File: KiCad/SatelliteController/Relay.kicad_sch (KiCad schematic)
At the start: 47 parts, among them J1 RELAY_POWER, J13 CONN_SORENOID_VALVE, Q10 AO3400A, Q11 AO3400A, Q12 AO3400A, Q4 AO3400A, Q5 AO3400A, Q6 AO3400A, Q7 AO3400A, Q8 AO3400A, Q9 AO3400A, U9 MCP3208

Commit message: ガーバーファイルを再生成
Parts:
- J13: footprint TSRP_Connector_Hirose:DF11B-8DP-2DS -> TSRP_Connector_Hirose:DF51A-8DP-2DS
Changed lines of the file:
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@@
       (effects (font (size 1.27 1.27)))
     )
-    (property "Footprint" "TSRP_Connector_Hirose:DF11B-8DP-2DS" (at 62.23 74.93 0)
+    (property "Footprint" "TSRP_Connector_Hirose:DF51A-8DP-2DS" (at 62.23 74.93 0)
       (effects (font (size 1.27 1.27)) hide)
     )

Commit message: 抵抗値を修正
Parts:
- R23: value 200R -> 120R
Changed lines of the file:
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@@
       (effects (font (size 1.27 1.27)))
     )
-    (property "Value" "200R" (at 39.37 36.83 90)
+    (property "Value" "120R" (at 39.37 36.83 90)
       (effects (font (size 1.27 1.27)))
     )
@@
       (effects (font (size 1.27 1.27)))
     )
-    (property "Value" "200R" (at 171.45 115.57 90)
+    (property "Value" "120R" (at 171.45 115.57 90)
       (effects (font (size 1.27 1.27)))
     )
@@
       (effects (font (size 1.27 1.27)))
     )
-    (property "Value" "200R" (at 106.68 53.34 90)
+    (property "Value" "120R" (at 106.68 53.34 90)
       (effects (font (size 1.27 1.27)))
     )
@@
       (effects (font (size 1.27 1.27)))
     )
-    (property "Value" "200R" (at 171.45 53.34 90)
+    (property "Value" "120R" (at 171.45 53.34 90)
       (effects (font (size 1.27 1.27)))
     )
@@
       (effects (font (size 1.27 1.27)))
     )
-    (property "Value" "200R" (at 232.41 115.57 90)
+    (property "Value" "120R" (at 232.41 115.57 90)
       (effects (font (size 1.27 1.27)))
     )
@@
       (effects (font (size 1.27 1.27)))
     )
-    (property "Value" "200R" (at 128.27 170.18 90)
+    (property "Value" "120R" (at 128.27 170.18 90)
       (effects (font (size 1.27 1.27)))
     )
@@
       (effects (font (size 1.27 1.27)))
     )
-    (property "Value" "200R" (at 232.41 53.34 90)
+    (property "Value" "120R" (at 232.41 53.34 90)
       (effects (font (size 1.27 1.27)))
     )
@@
       (effects (font (size 1.27 1.27)))
     )
-    (property "Value" "200R" (at 106.68 115.57 90)
+    (property "Value" "120R" (at 106.68 115.57 90)
       (effects (font (size 1.27 1.27)))
     )
@@
       (effects (font (size 1.27 1.27)))
     )
-    (property "Value" "200R" (at 69.85 170.18 90)
-      (effects (font (size 1.27 1.27)))
-    )
+    (property "Value" "120R" (at 69.85 170.18 90)
+      (effects (font (size 1.27 1.27)))
+    )

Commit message: サテコンの制御スイッチをプルダウンに変更
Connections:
- net CTL_PURGE renamed LED_PURGE
- net CTL_SAFETY renamed LED_SAFTEY
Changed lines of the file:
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@@
+    (stroke (width 0) (type default))
+  )
+  (wire (pts (xy 34.29 39.37) (xy 36.83 39.37))
     (stroke (width 0) (type default))
   )
@@
     (stroke (width 0) (type default))
   )
-  (wire (pts (xy 34.29 39.37) (xy 36.83 39.37))
-    (stroke (width 0) (type default))
-  )
   (wire (pts (xy 62.23 106.68) (xy 64.77 106.68))
     (stroke (width 0) (type default))
@@
     )
   )
-  (global_label "CTL_SAFETY" (shape input) (at 34.29 39.37 180) (fields_autoplaced)
-    (effects (font (size 1.27 1.27)) (justify right))
-    (property "Intersheetrefs" "${INTERSHEET_REFS}" (at 20.559 39.37 0)
-      (effects (font (size 1.27 1.27)) (justify right) hide)
-    )
-  )
   (global_label "VREF_FILL" (shape output) (at 184.15 38.1 180) (fields_autoplaced)
     (effects (font (size 1.27 1.27)) (justify right))
@@
     )
   )
+  (global_label "LED_PURGE" (shape input) (at 123.19 172.72 180) (fields_autoplaced)
+    (effects (font (size 1.27 1.27)) (justify right))
+    (property "Intersheetrefs" "${INTERSHEET_REFS}" (at 109.58 172.72 0)
+      (effects (font (size 1.27 1.27)) (justify right) hide)
+    )
+  )
   (global_label "CTL_OPEN" (shape input) (at 227.33 118.11 180) (fields_autoplaced)
     (effects (font (size 1.27 1.27)) (justify right))
@@
     )
   )
+  (global_label "LED_SAFTEY" (shape input) (at 34.29 39.37 180) (fields_autoplaced)
+    (effects (font (size 1.27 1.27)) (justify right))
+    (property "Intersheetrefs" "${INTERSHEET_REFS}" (at 20.3776 39.37 0)
+      (effects (font (size 1.27 1.27)) (justify right) hide)
+    )
+  )
   (global_label "SPI_SCK" (shape input) (at 64.77 106.68 0) (fields_autoplaced)
     (effects (font (size 1.27 1.27)) (justify left))
@@
       (effects (font (size 1.27 1.27)) (justify right) hide)
     )
-  )
-  (global_label "CTL_PURGE" (shape input) (at 123.19 172.72 180) (fields_autoplaced)
-    (effects (font (size 1.27 1.27)) (justify right))
-    (property "Intersheetrefs" "${INTERSHEET_REFS}" (at 109.7614 172.72 0)
-      (effects (font (size 1.27 1.27)) (justify right) hide)
-    )

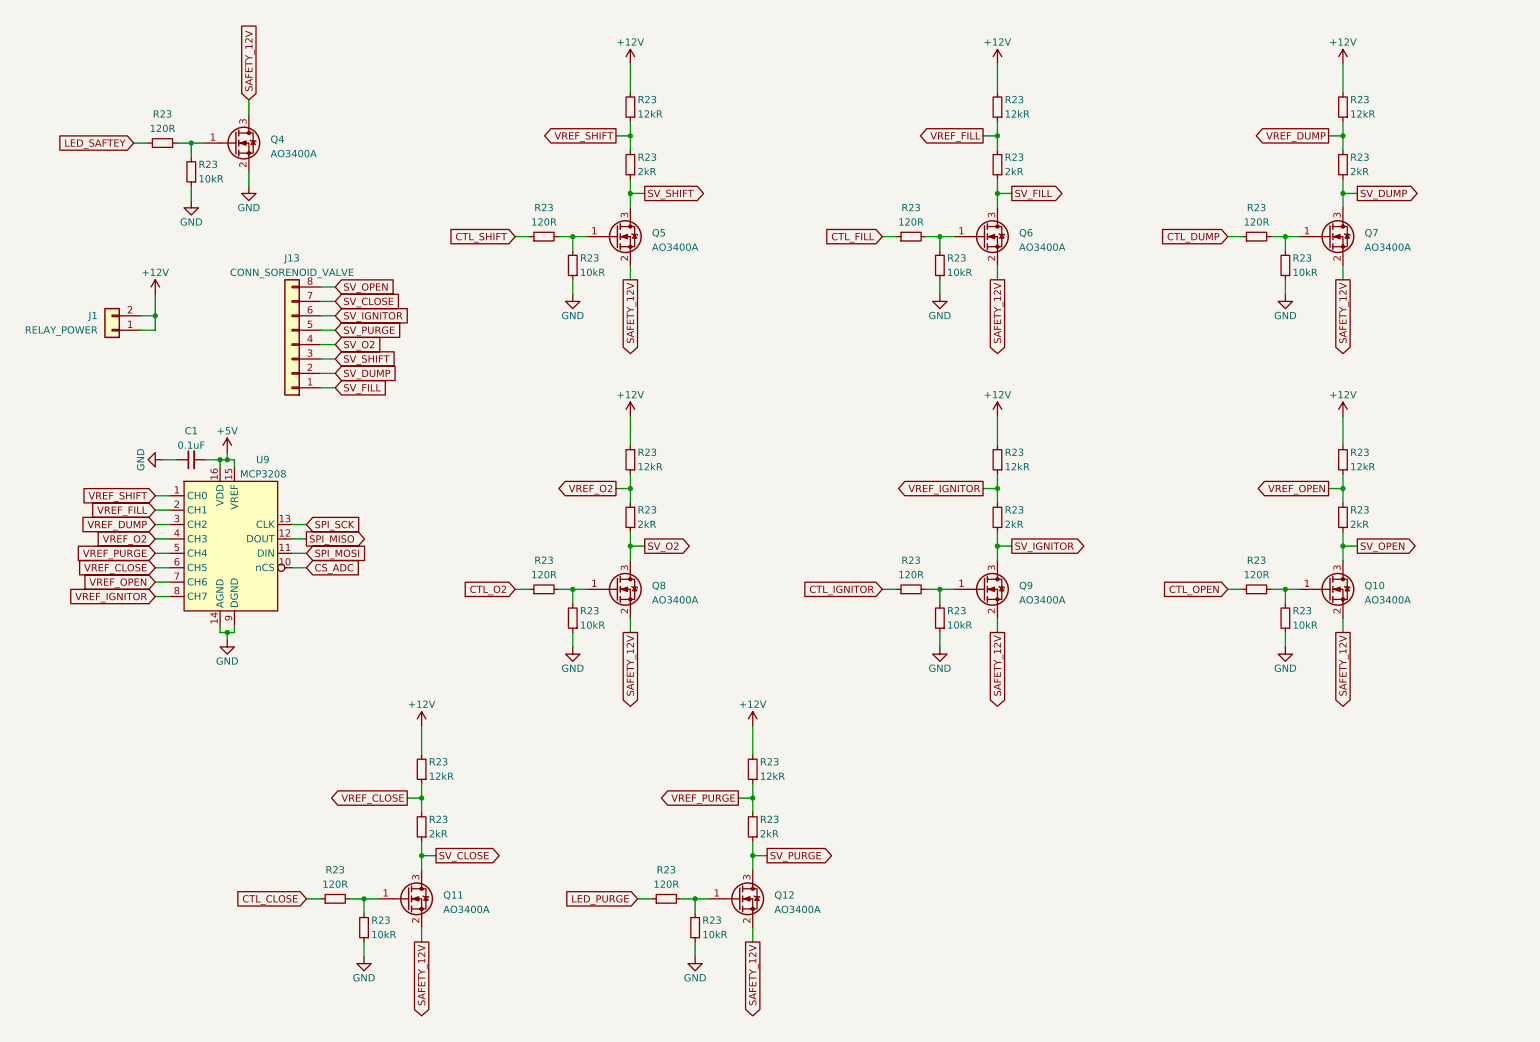
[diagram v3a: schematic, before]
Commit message: サテコンのオープン検知を修正
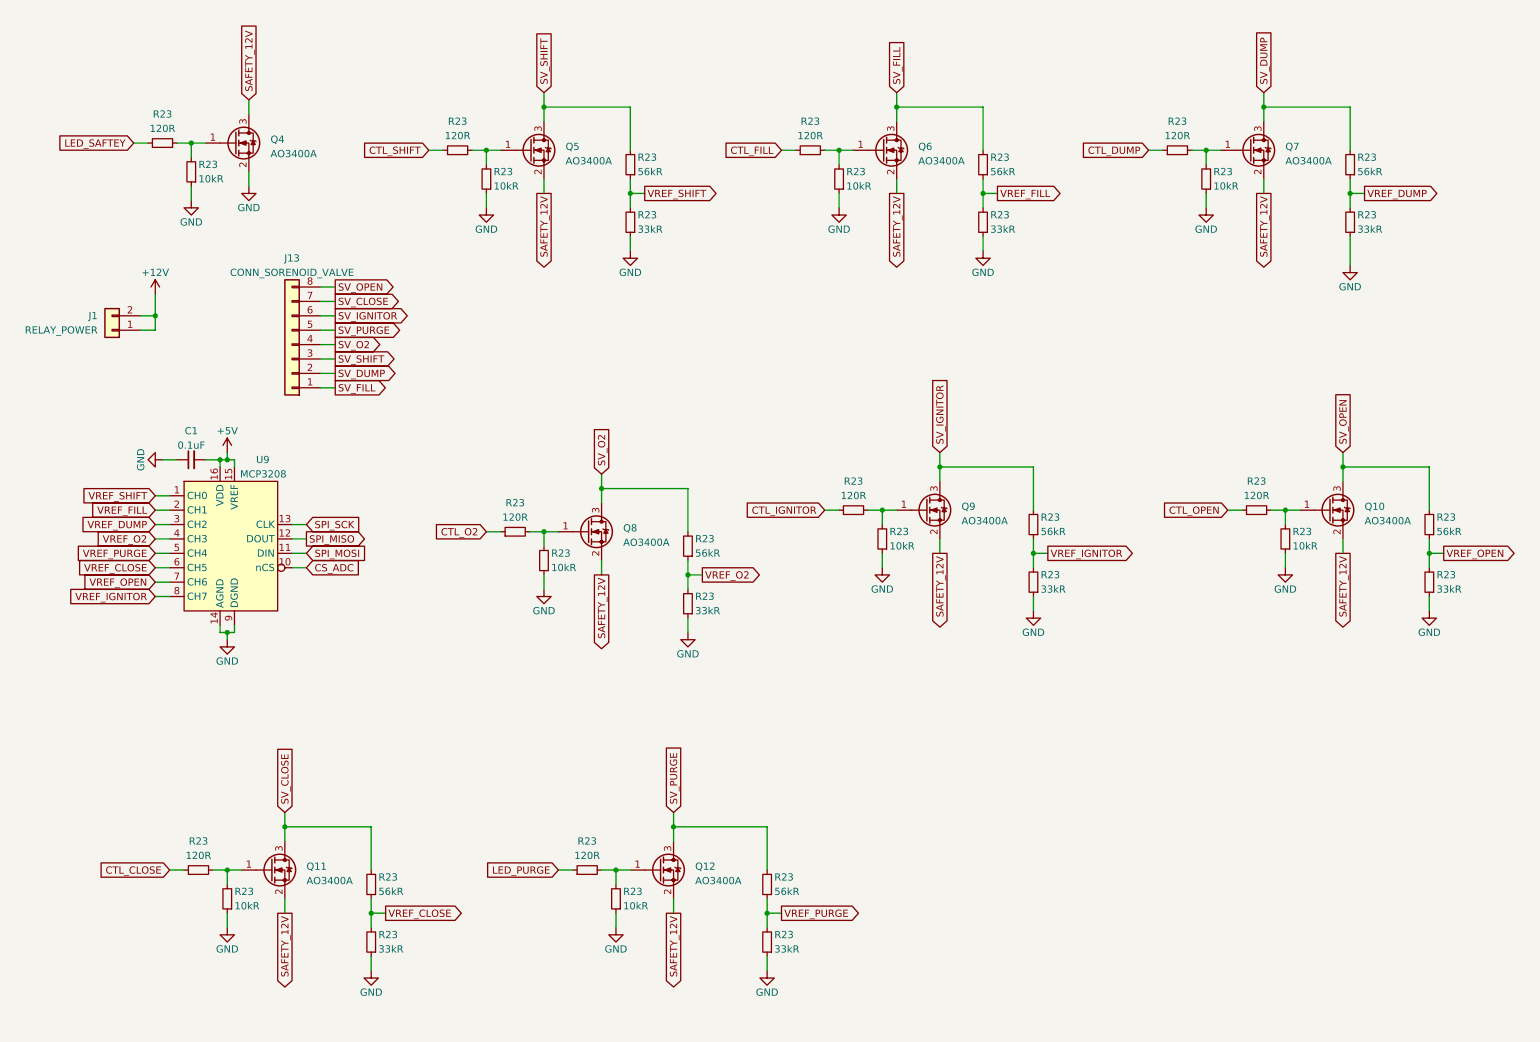
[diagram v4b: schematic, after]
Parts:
- R23: value 2kR -> 33kR
- R23: value 12kR -> 56kR
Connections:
- net +12V: no longer R23.2, R23.2, R23.2, R23.2, R23.2, R23.2, R23.2, R23.2
- net GND: now also R23.1, R23.1, R23.1, R23.1, R23.1, R23.1, R23.1, R23.1
- net SV_CLOSE: now also R23.2; no longer R23.1
- net SV_DUMP: now also R23.2; no longer R23.1
- net SV_FILL: now also R23.2; no longer R23.1
- net SV_IGNITOR: now also R23.2; no longer R23.1
- net SV_O2: now also R23.2; no longer R23.1
- net SV_OPEN: now also R23.2; no longer R23.1
- net SV_PURGE: now also R23.2; no longer R23.1
- net SV_SHIFT: now also R23.2; no longer R23.1
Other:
- moved on the sheet: Q10, Q11, Q12, Q5, Q6, Q7, Q8, Q9, R23

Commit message: サテコンのクリスマスツリーを削除
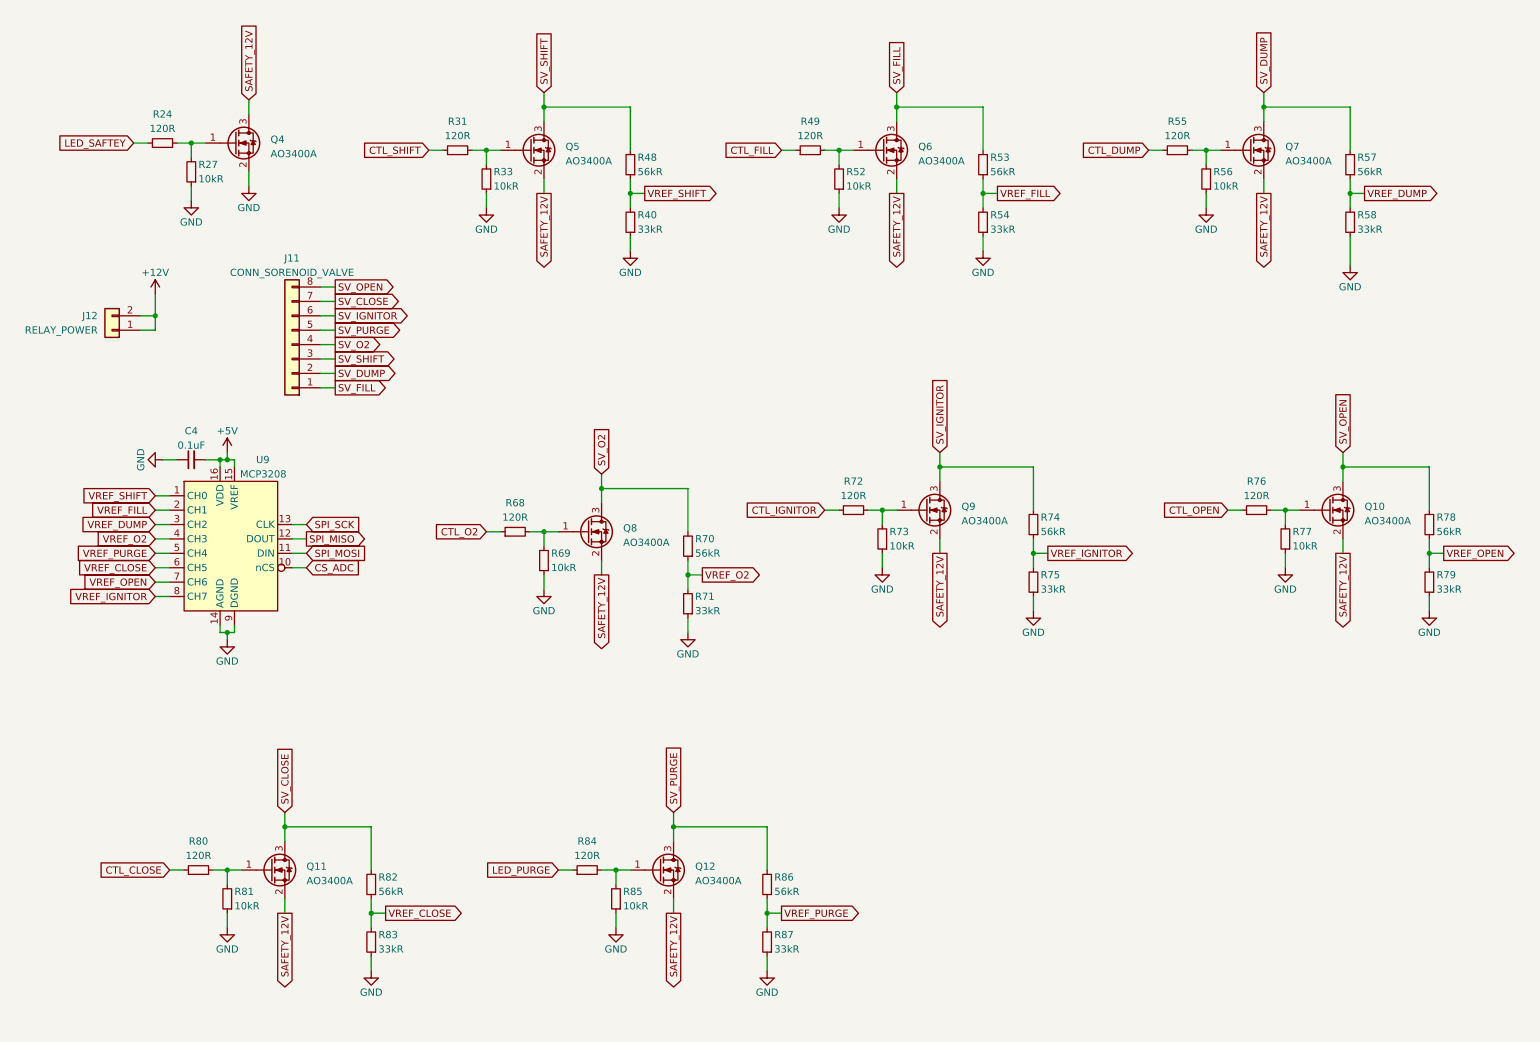
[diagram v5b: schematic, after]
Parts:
- renumbered C1 to C4, J13 to J11, J1 to J12, R23 to R24, R23 to R27, R23 to R31, R23 to R33, R23 to R40, R23 to R48, R23 to R49, R23 to R52, R23 to R53, R23 to R54, R23 to R55, R23 to R56, R23 to R57, R23 to R58, R23 to R68, R23 to R69, R23 to R70, R23 to R71, R23 to R72, R23 to R73, R23 to R74, R23 to R75, R23 to R76, R23 to R77, R23 to R78, R23 to R79, R23 to R80, R23 to R81, R23 to R82, R23 to R83, R23 to R84, R23 to R85, R23 to R86, R23 to R87

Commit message: 電磁弁制御回路を整理
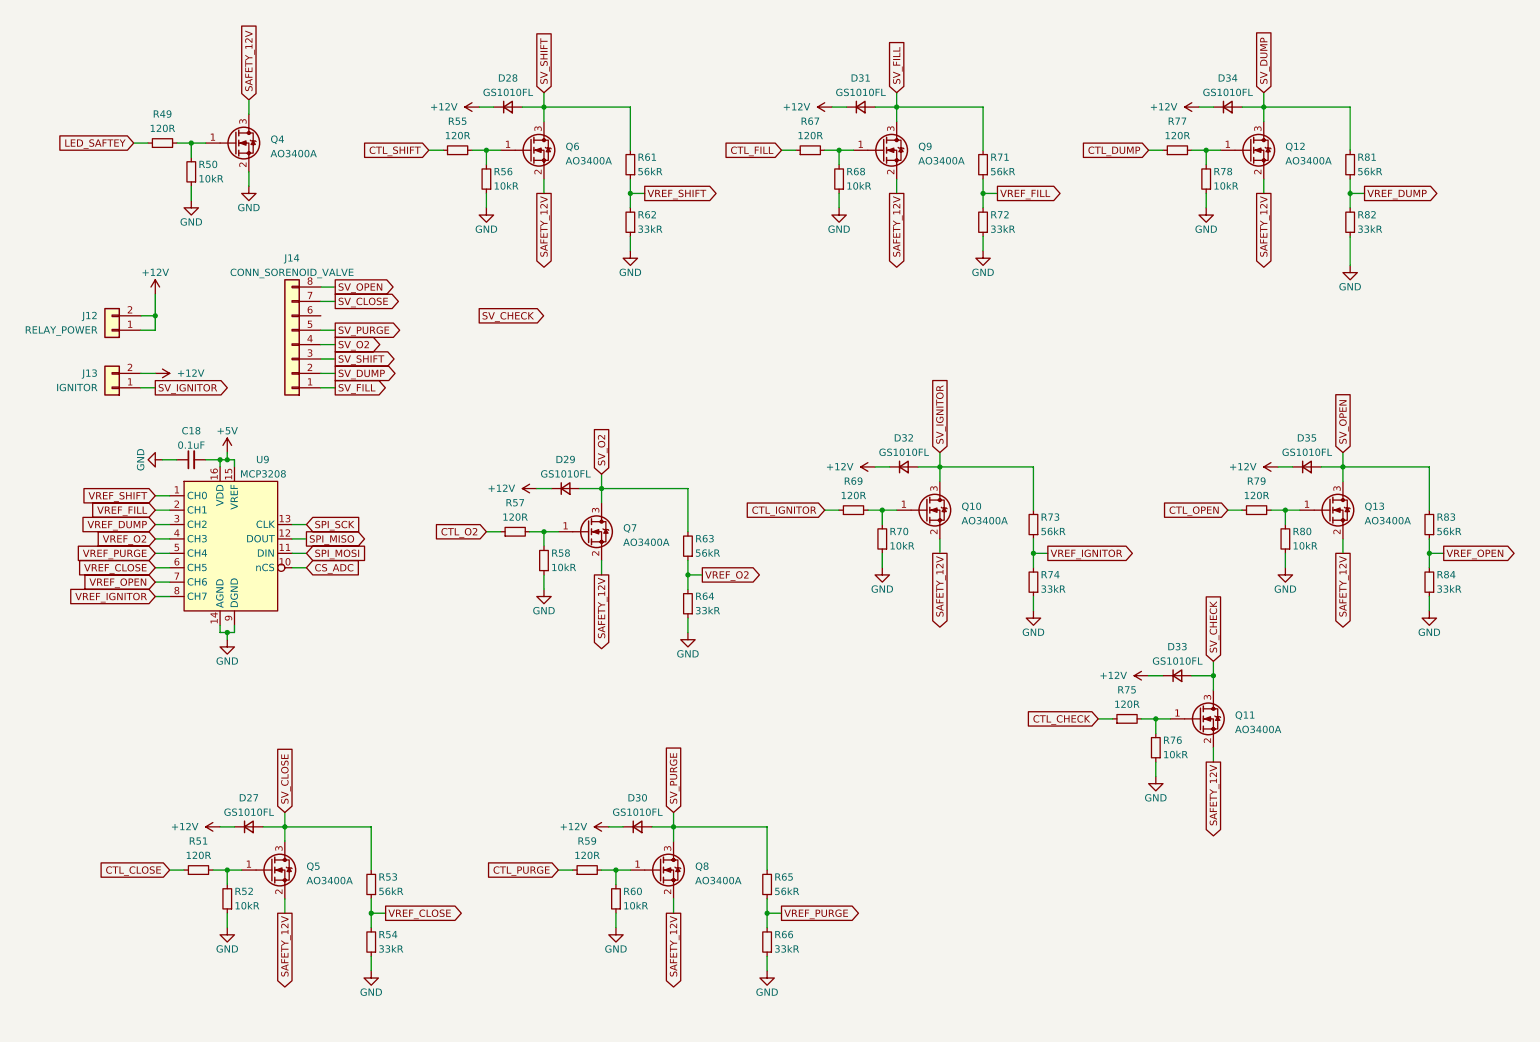
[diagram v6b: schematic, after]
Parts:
- added D27, D28, D29, D30, D31, D32, D33, D34, D35: GS1010FL, Diode_SMD:D_SOD-123F, symbol Device:D_Small
- added J13: IGNITOR, TSRP_Connector_Hirose:DF51-2P-2DS, symbol Connector_Generic:Conn_01x02
- added Q11: AO3400A, Package_TO_SOT_SMD:SOT-23, symbol Transistor_FET:AO3400A
- added R75: 120R, Resistor_SMD:R_0603_1608Metric_Pad0.98x0.95mm_HandSolder, symbol Device:R_Small
- added R76: 10kR, Resistor_SMD:R_0603_1608Metric_Pad0.98x0.95mm_HandSolder, symbol Device:R_Small
- renumbered C4 to C18, J11 to J14, Q9 to Q10, Q7 to Q12, Q10 to Q13, Q11 to Q5, Q5 to Q6, Q8 to Q7, Q12 to Q8, Q6 to Q9, R24 to R49, R27 to R50, R80 to R51, R81 to R52, R82 to R53, R83 to R54, R31 to R55, R33 to R56, R68 to R57, R69 to R58, R84 to R59, R85 to R60, R48 to R61, R40 to R62, R70 to R63, R71 to R64, R86 to R65, R87 to R66, R49 to R67, R52 to R68, R72 to R69, R73 to R70, R53 to R71, R54 to R72, R74 to R73, R75 to R74, R55 to R77, R56 to R78, R76 to R79, R77 to R80, R57 to R81, R58 to R82, R78 to R83, R79 to R84
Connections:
- net +12V: now also D27.1 (K), D28.1 (K), D29.1 (K), D30.1 (K), D31.1 (K), D32.1 (K), D33.1 (K), D34.1 (K), D35.1 (K), J13.2 (Pin_2)
- net GND: now also R76.1
- net SAFETY_12V: now also Q11.2 (S)
- net SV_CLOSE: now also D27.2 (A)
- net SV_DUMP: now also D34.2 (A)
- net SV_FILL: now also D31.2 (A)
- net SV_IGNITOR: now also D32.2 (A), J13.1 (Pin_1); no longer J14.6 (Pin_6)
- net SV_O2: now also D29.2 (A)
- net SV_OPEN: now also D35.2 (A)
- net SV_PURGE: now also D30.2 (A)
- net SV_SHIFT: now also D28.2 (A)
- net LED_PURGE renamed CTL_PURGE
- new net: Q11.1 (G), R75.2, R76.2
- new net CTL_CHECK: R75.1
- new net SV_CHECK: D33.2 (A), Q11.3 (D)

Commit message: 配線
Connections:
- net SV_CHECK: now also J14.6 (Pin_6)
- net SV_DUMP: now also J14.1 (Pin_1); no longer J14.2 (Pin_2)
- net SV_FILL: now also J14.2 (Pin_2); no longer J14.1 (Pin_1)
- net SV_O2: now also J14.3 (Pin_3); no longer J14.4 (Pin_4)
- net SV_OPEN: now also J14.5 (Pin_5); no longer J14.8 (Pin_8)
- net SV_PURGE: now also J14.8 (Pin_8); no longer J14.5 (Pin_5)
- net SV_SHIFT: now also J14.4 (Pin_4); no longer J14.3 (Pin_3)

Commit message: ガーバーを出力
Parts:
- J13: footprint TSRP_Connector_Hirose:DF51-2P-2DS -> TSRP_TerminalBlock_Alphaplus:TB411-2-2-E-1
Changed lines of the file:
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@@
 			)
 		)
-		(property "Footprint" "TSRP_Connector_Hirose:DF51-2P-2DS"
+		(property "Footprint" "TSRP_TerminalBlock_Alphaplus:TB411-2-2-E-1"
 			(at 30.48 82.55 0)
 			(effects
